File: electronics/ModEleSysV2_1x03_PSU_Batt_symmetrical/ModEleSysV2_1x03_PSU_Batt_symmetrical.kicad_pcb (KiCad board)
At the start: 2 copper layers, 22.8 x 48.6 mm, 18 parts, among them J2 Conn_01x02, J3 Conn_01x02, J4 Conn_01x03, SW1 switch_DPDT, U1 TSC432

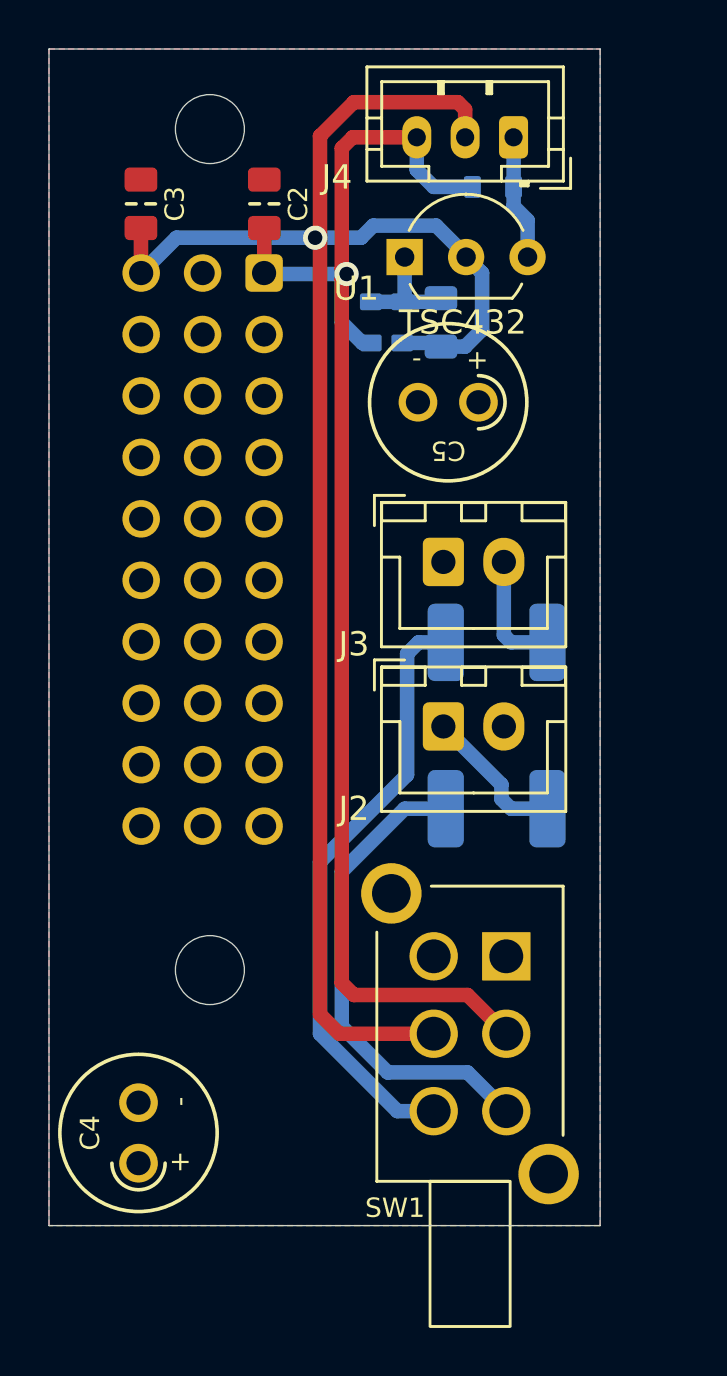
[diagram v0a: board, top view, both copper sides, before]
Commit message: silk placement done, ready for review
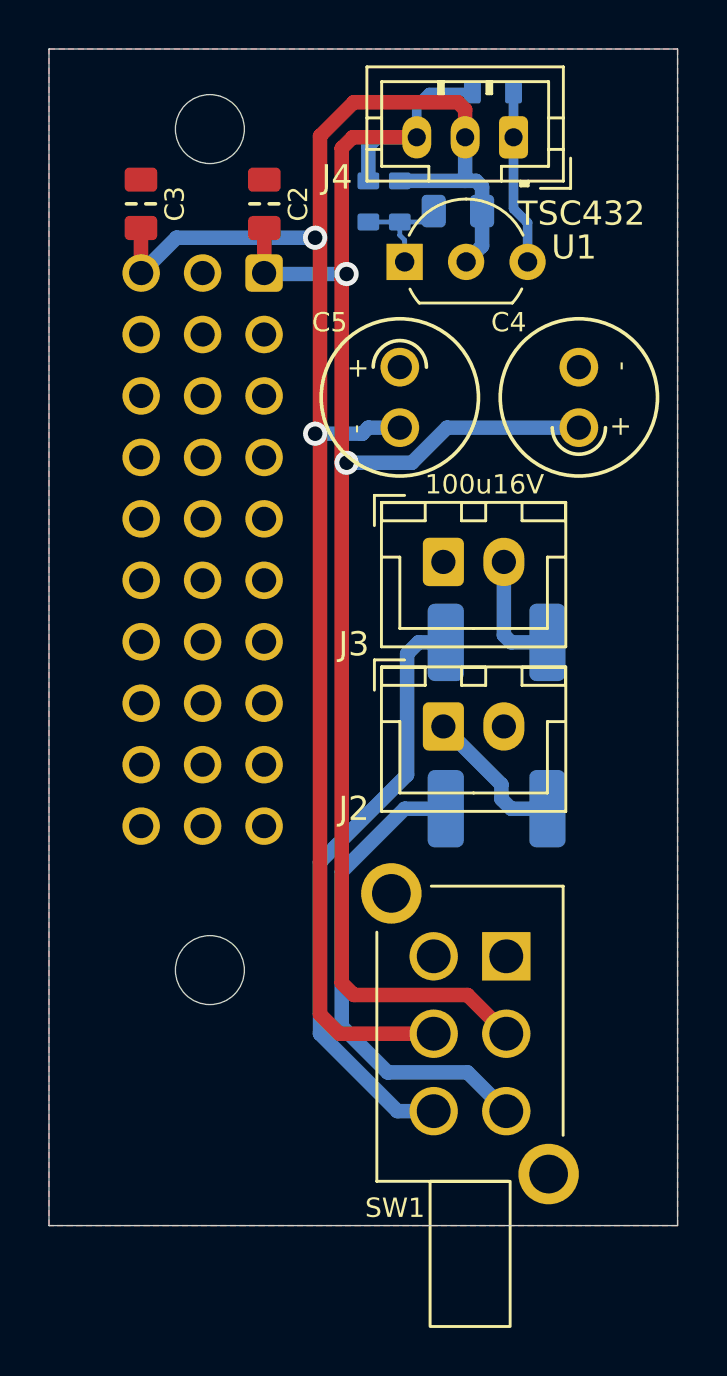
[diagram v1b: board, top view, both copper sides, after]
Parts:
- C4, C5: value C_Polarized -> 100u16V
- moved C4 35.4 mm to (161.6, 78.8)
- moved R2 5.00 mm to (154.2, 70.7), turned to -90 degrees
- moved R3 5.00 mm to (152.9, 70.7), turned to -90 degrees
- moved C1 4.65 mm to (156.6, 71.1), turned to 0 degrees
- moved R1 3.90 mm to (158.1, 66.2)
- moved C5 2.01 mm to (154.2, 78.8), turned to -90 degrees
- moved U1 0.20 mm to (154.4, 73.2)
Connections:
- C4 pad 1: unconnected-(C4-Pad1) -> /+aV
- C4 pad 2: unconnected-(C4-Pad2) -> GND
- C5 pad 1: unconnected-(C5-Pad1) -> GND
- C5 pad 2: unconnected-(C5-Pad2) -> /-aV
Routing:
- net /+aV: track 58.5 -> 68.8 mm, vias 1 -> 2
- net /lowBatt: track 5.19 -> 7.24 mm
- net /-aV: track 73.0 -> 71.8 mm, vias 1 -> 2
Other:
- board size 22.8 x 48.6 mm -> 26 x 48.6 mm

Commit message: reviewed
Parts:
- C2, C3: footprint SquantorCapacitor:C_0805 -> SquantorCapacitor:C_1206_0805
- N1: value 20240311 -> 20240424
- moved C2 1.44 mm to (149.4, 69.6)
- moved C3 1.22 mm to (143.3, 69.6)
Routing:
- net GND: vias 0 -> 2

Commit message: updated versionnumbers
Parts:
- N1: value 20240424 -> 20240426
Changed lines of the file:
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@@
         (effects (font (size 1 1) (thickness 0.15)) (justify mirror))
     )
-    (fp_text value "20240424" (at 0.8 0.1 90) (layer "B.SilkS")
+    (fp_text value "20240426" (at 0.8 0.1 90) (layer "B.SilkS")
         (effects (font (size 0.8 0.8) (thickness 0.15)) (justify mirror))
     )
@@
         (effects (font (size 0.8 0.8) (thickness 0.15)) (justify mirror))
     )
-    (fp_text value "0.6A 60V" (at 0 4.375 unlocked) (layer "B.Fab")
+    (fp_text value "0.6A 60V" (at 0 -2.6 unlocked) (layer "B.SilkS")
         (effects (font (size 0.8 0.8) (thickness 0.15)) (justify mirror))
     )
@@
     (property "ki_keywords" "cap capacitor")
     (attr smd)
-    (fp_text reference "C1" (at 2.5 0 180) (layer "B.SilkS")
-        (effects (font (size 0.8 0.8) (thickness 0.15)) (justify mirror))
-    )
-    (fp_text value "2.2u" (at 4.7 0) (layer "B.SilkS")
+    (fp_text reference "C1" (at 5.8 0 180) (layer "B.SilkS")
+        (effects (font (size 0.8 0.8) (thickness 0.15)) (justify mirror))
+    )
+    (fp_text value "2.2u" (at 3 0) (layer "B.SilkS")
         (effects (font (size 0.8 0.8) (thickness 0.15)) (justify mirror))
     )
@@
     (property "ki_keywords" "R res resistor")
     (attr smd)
-    (fp_text reference "R1" (at 2.15 0) (layer "B.SilkS")
-        (effects (font (size 0.8 0.8) (thickness 0.15)) (justify mirror))
-    )
-    (fp_text value "2.2K" (at 4.35 0) (layer "B.SilkS")
+    (fp_text reference "R1" (at 5.15 0) (layer "B.SilkS")
+        (effects (font (size 0.8 0.8) (thickness 0.15)) (justify mirror))
+    )
+    (fp_text value "2.2K" (at 2.75 0) (layer "B.SilkS")
         (effects (font (size 0.8 0.8) (thickness 0.15)) (justify mirror))
     )
@@
         (effects (font (size 0.8 0.8) (thickness 0.15)) (justify mirror))
     )
-    (fp_text value "0.6A 60V" (at 0 -2.6 unlocked) (layer "B.Fab")
-        (effects (font (size 0.8 0.8) (thickness 0.15)) (justify mirror))
-    )
+    (fp_text value "0.6A 60V" (at 0 -2.175 unlocked) (layer "B.Fab")
+        (effects (font (size 0.8 0.8) (thickness 0.15)) (justify mirror))
+    )
